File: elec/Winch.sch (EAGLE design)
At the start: 7 parts, among them IC1 LM311D

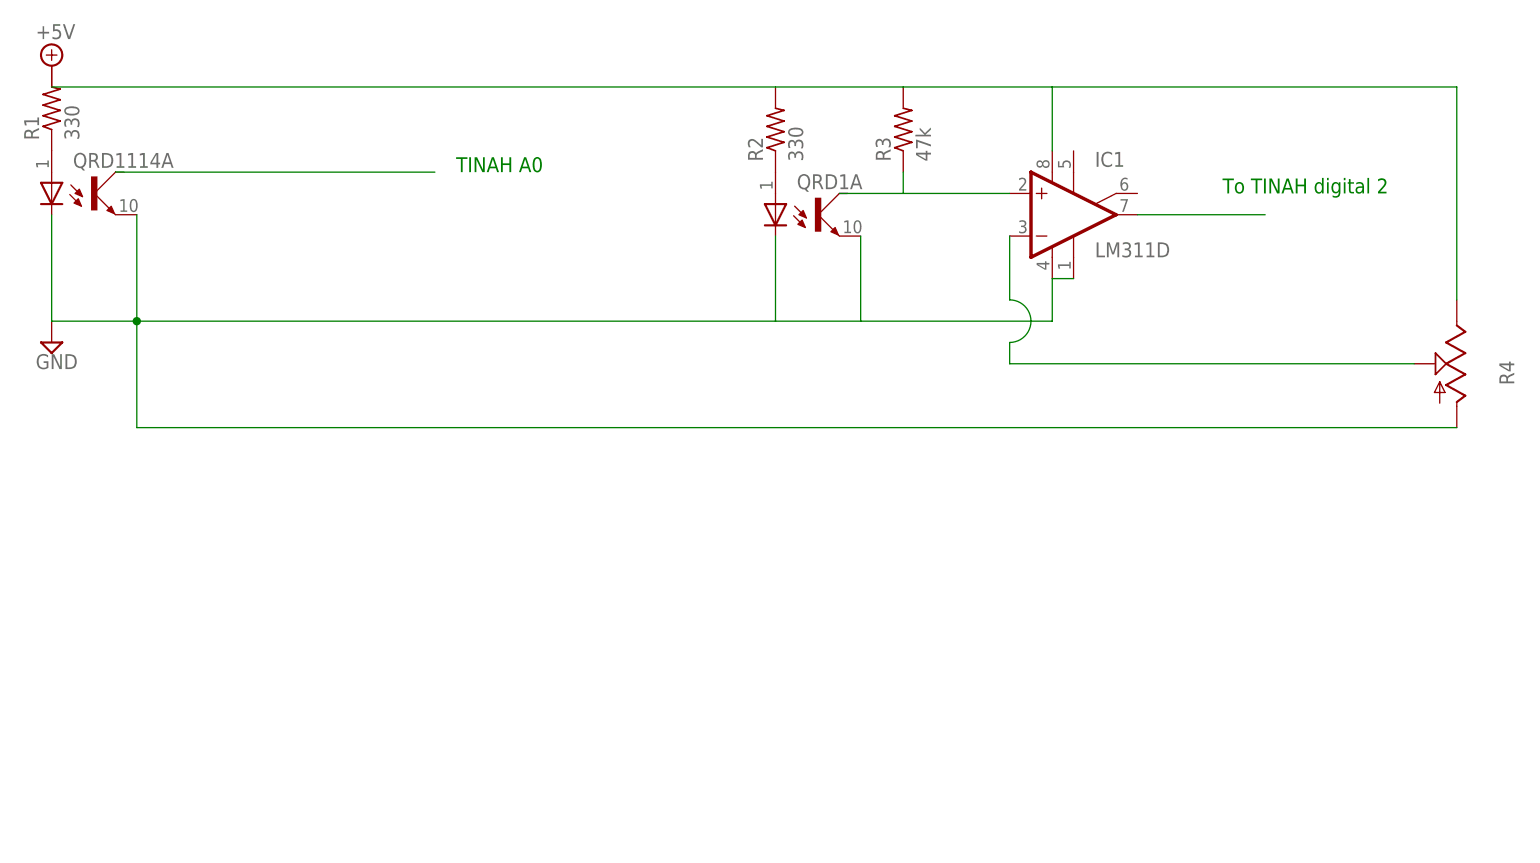
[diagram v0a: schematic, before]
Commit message: Updated QRD and created winch circuit
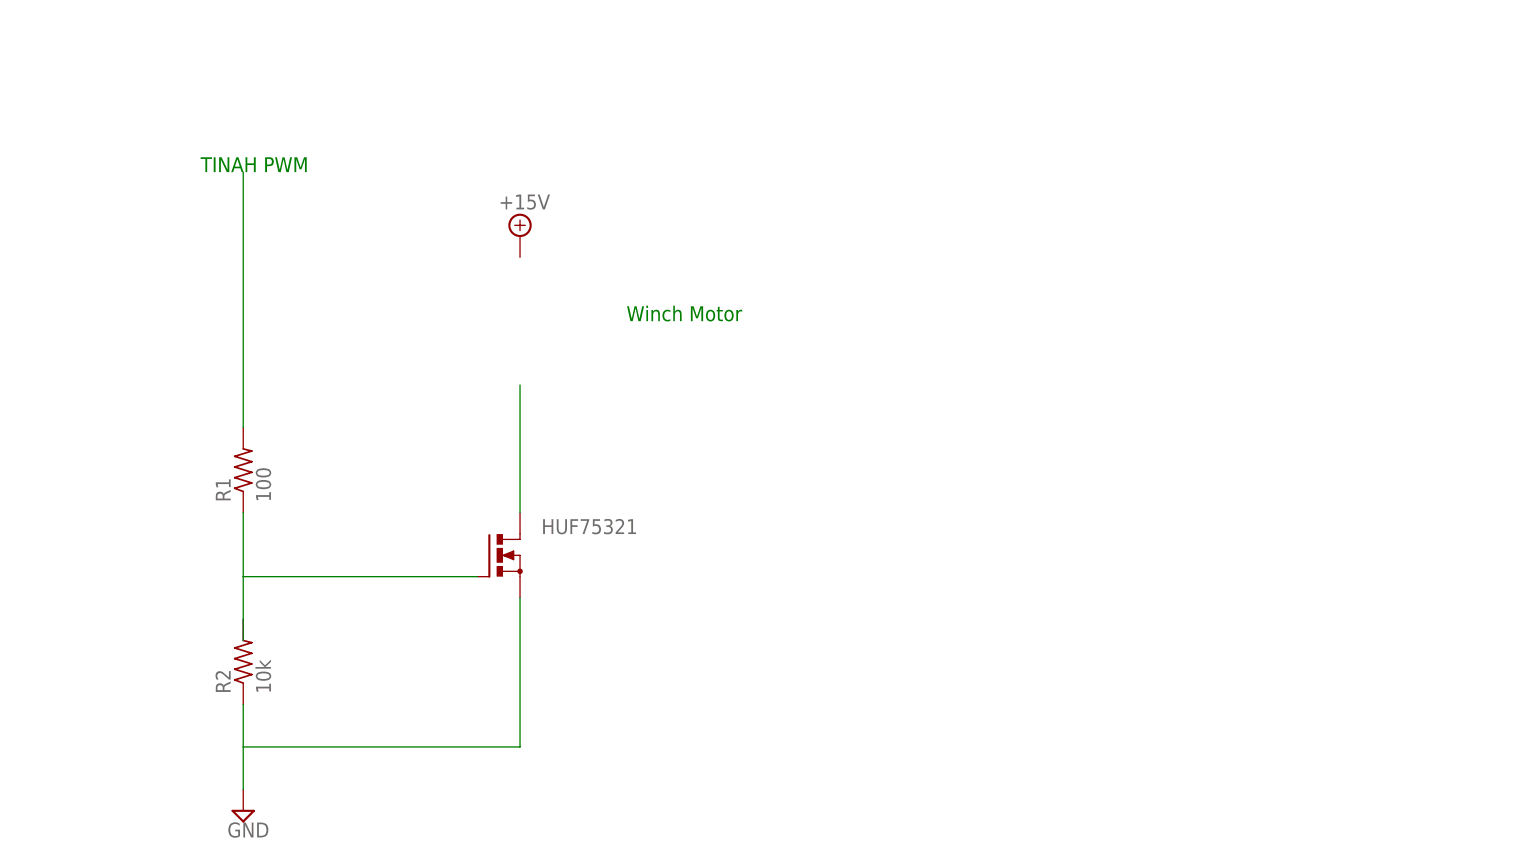
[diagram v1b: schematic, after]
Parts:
- removed IC1: LM311D, linear:LM311D
- removed QRD1, QRD1114: SFH6943, opto-vishay:SFH6943
- removed R3: 47k, resistor:R-US_0204/2V
- removed R4: (no value), pot:TRIM_US-3223G
- added HUF75321: (no value), transistor-power:N-MOSFET-SO8S
- R1: value 330 -> 100
- R2: value 330 -> 10k
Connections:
- removed net +5V: IC1.V+, R2.2, R3.2, R4.E
- removed net N$4: IC1.-IN, R4.S
- removed net N$5: IC1.+IN, R3.1
- removed net N$7: IC1.OUT
- new net N$1: R1.2
- net GND: now also HUF75321.S, R2.1; no longer IC1.GND, IC1.V-, QRD1114A.EMI, QRD1A.EMI, R4.A
- net N$2: now also HUF75321.G, R2.2; no longer QRD1114A.A
- net N$3: now also HUF75321.D; no longer QRD1A.A, R2.1
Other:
- note added: "TINAH PWM"
- note added: "Winch Motor"
- note removed: "TINAH A0"
- note removed: "To TINAH digital 2"
- moved on the sheet: R1, R2
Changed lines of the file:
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@@
 <layer number="48" name="Document" color="7" fill="1" visible="no" active="no"/>
 <layer number="49" name="Reference" color="7" fill="1" visible="no" active="no"/>
-<layer number="51" name="tDocu" color="6" fill="1" visible="no" active="no"/>
+<layer number="51" name="tDocu" color="7" fill="1" visible="no" active="no"/>
 <layer number="52" name="bDocu" color="7" fill="1" visible="no" active="no"/>
-<layer number="57" name="t3D" color="6" fill="5" visible="no" active="no"/>
-<layer number="58" name="b3D" color="5" fill="4" visible="no" active="no"/>
 <layer number="90" name="Modules" color="5" fill="1" visible="yes" active="yes"/>
 <layer number="91" name="Nets" color="2" fill="1" visible="yes" active="yes"/>
@@
 </classes>
 <parts>
-<part name="QRD1114" library="opto-vishay" deviceset="SFH6943" device="" value=""/>
+<part name="R1" library="resistor" deviceset="R-US_" device="0204/2V" value="100"/>
+<part name="R2" library="resistor" deviceset="R-US_" device="0204/2V" value="10k"/>
 <part name="SUPPLY1" library="supply2" deviceset="GND" device=""/>
-<part name="R1" library="resistor" deviceset="R-US_" device="0204/2V" value="330"/>
-<part name="SUPPLY2" library="supply2" deviceset="+5V" device=""/>
-<part name="R2" library="resistor" deviceset="R-US_" device="0204/2V" value="330"/>
-<part name="QRD1" library="opto-vishay" deviceset="SFH6943" device="" value=""/>
-<part name="R3" library="resistor" deviceset="R-US_" device="0204/2V" value="47k"/>
-<part name="IC1" library="linear" deviceset="LM311" device="D"/>
-<part name="R4" library="pot" deviceset="TRIM_US-" device="3223G"/>
+<part name="HUF75321" library="transistor-power" deviceset="N-MOSFET-SO8" device="S"/>
+<part name="SUPPLY2" library="supply2" deviceset="+15V" device=""/>
 </parts>
 <sheets>
 <sheet>
 <plain>
-<text x="20.32" y="86.36" size="1.778" layer="91">TINAH A0</text>
-<text x="111.76" y="83.82" size="1.778" layer="91">To TINAH digital 2</text>
+<text x="-10.16" y="86.36" size="1.778" layer="91">TINAH PWM</text>
+<circle x="27.94" y="68.58" radius="8.032184375" width="0.1524" layer="99"/>
+<text x="40.64" y="68.58" size="1.778" layer="91">Winch Motor</text>
 </plain>
 <instances>
-<instance part="QRD1114" gate="A" x="-27.94" y="83.82"/>
-<instance part="SUPPLY1" gate="GND" x="-27.94" y="66.04"/>
-<instance part="R1" gate="G$1" x="-27.94" y="93.98" rot="R90"/>
-<instance part="SUPPLY2" gate="+5V" x="-27.94" y="99.06"/>
-<instance part="R2" gate="G$1" x="58.42" y="91.44" rot="R90"/>
-<instance part="QRD1" gate="A" x="58.42" y="81.28"/>
-<instance part="R3" gate="G$1" x="73.66" y="91.44" rot="R90"/>
-<instance part="IC1" gate="A" x="93.98" y="81.28"/>
-<instance part="R4" gate="G$1" x="139.7" y="63.5" rot="MR0"/>
+<instance part="R1" gate="G$1" x="-5.08" y="50.8" rot="R90"/>
+<instance part="R2" gate="G$1" x="-5.08" y="27.94" rot="R90"/>
+<instance part="SUPPLY1" gate="GND" x="-5.08" y="10.16"/>
+<instance part="HUF75321" gate="G$1" x="25.4" y="40.64"/>
+<instance part="SUPPLY2" gate="+15V" x="27.94" y="78.74"/>
 </instances>
 <busses>
@@
 <net name="N$1" class="0">
 <segment>
-<wire x1="-20.32" y1="86.36" x2="17.78" y2="86.36" width="0.1524" layer="91"/>
+<wire x1="-5.08" y1="86.36" x2="-5.08" y2="55.88" width="0.1524" layer="91"/>
+<pinref part="R1" gate="G$1" pin="2"/>
+</segment>
+</net>
+<net name="N$2" class="0">
+<segment>
+<pinref part="R1" gate="G$1" pin="1"/>
+<pinref part="R2" gate="G$1" pin="2"/>
+<wire x1="-5.08" y1="45.72" x2="-5.08" y2="38.1" width="0.1524" layer="91"/>
+<wire x1="-5.08" y1="38.1" x2="-5.08" y2="33.02" width="0.1524" layer="91"/>
+<wire x1="-5.08" y1="33.02" x2="-5.08" y2="30.48" width="0.1524" layer="91"/>
+<pinref part="HUF75321" gate="G$1" pin="G"/>
+<wire x1="-5.08" y1="38.1" x2="22.86" y2="38.1" width="0.1524" layer="91"/>
 </segment>
 </net>
 <net name="GND" class="0">
 <segment>
+<pinref part="R2" gate="G$1" pin="1"/>
 <pinref part="SUPPLY1" gate="GND" pin="GND"/>
-<wire x1="-27.94" y1="81.28" x2="-27.94" y2="68.58" width="0.1524" layer="91"/>
-<pinref part="QRD1114" gate="A" pin="EMI"/>
-<wire x1="-27.94" y1="68.58" x2="-17.78" y2="68.58" width="0.1524" layer="91"/>
-<wire x1="-17.78" y1="68.58" x2="-17.78" y2="81.28" width="0.1524" layer="91"/>
-<wire x1="58.42" y1="78.74" x2="58.42" y2="68.58" width="0.1524" layer="91"/>
-<wire x1="58.42" y1="68.58" x2="-17.78" y2="68.58" width="0.1524" layer="91"/>
-<pinref part="QRD1" gate="A" pin="EMI"/>
-<wire x1="58.42" y1="68.58" x2="68.58" y2="68.58" width="0.1524" layer="91"/>
-<wire x1="68.58" y1="68.58" x2="68.58" y2="78.74" width="0.1524" layer="91"/>
-<pinref part="IC1" gate="A" pin="V-"/>
-<pinref part="IC1" gate="A" pin="GND"/>
-<wire x1="93.98" y1="73.66" x2="91.44" y2="73.66" width="0.1524" layer="91"/>
-<wire x1="91.44" y1="73.66" x2="91.44" y2="68.58" width="0.1524" layer="91"/>
-<wire x1="91.44" y1="68.58" x2="68.58" y2="68.58" width="0.1524" layer="91"/>
-<pinref part="R4" gate="G$1" pin="A"/>
-<wire x1="139.7" y1="55.88" x2="-17.78" y2="55.88" width="0.1524" layer="91"/>
-<wire x1="-17.78" y1="55.88" x2="-17.78" y2="68.58" width="0.1524" layer="91"/>
-<junction x="-17.78" y="68.58"/>
-</segment>
-</net>
-<net name="N$2" class="0">
-<segment>
-<pinref part="QRD1114" gate="A" pin="A"/>
-<pinref part="R1" gate="G$1" pin="1"/>
-</segment>
-</net>
-<net name="+5V" class="0">
-<segment>
-<pinref part="SUPPLY2" gate="+5V" pin="+5V"/>
-<wire x1="-27.94" y1="96.52" x2="58.42" y2="96.52" width="0.1524" layer="91"/>
-<pinref part="R2" gate="G$1" pin="2"/>
-<pinref part="R3" gate="G$1" pin="2"/>
-<wire x1="58.42" y1="96.52" x2="73.66" y2="96.52" width="0.1524" layer="91"/>
-<pinref part="IC1" gate="A" pin="V+"/>
-<wire x1="73.66" y1="96.52" x2="91.44" y2="96.52" width="0.1524" layer="91"/>
-<wire x1="91.44" y1="96.52" x2="91.44" y2="88.9" width="0.1524" layer="91"/>
-<pinref part="R4" gate="G$1" pin="E"/>
-<wire x1="139.7" y1="71.12" x2="139.7" y2="96.52" width="0.1524" layer="91"/>
-<wire x1="139.7" y1="96.52" x2="91.44" y2="96.52" width="0.1524" layer="91"/>
+<wire x1="-5.08" y1="22.86" x2="-5.08" y2="17.78" width="0.1524" layer="91"/>
+<pinref part="HUF75321" gate="G$1" pin="S"/>
+<wire x1="-5.08" y1="17.78" x2="-5.08" y2="12.7" width="0.1524" layer="91"/>
+<wire x1="-5.08" y1="17.78" x2="27.94" y2="17.78" width="0.1524" layer="91"/>
+<wire x1="27.94" y1="17.78" x2="27.94" y2="35.56" width="0.1524" layer="91"/>
 </segment>
 </net>
 <net name="N$3" class="0">
 <segment>
-<pinref part="R2" gate="G$1" pin="1"/>
-<pinref part="QRD1" gate="A" pin="A"/>
+<pinref part="HUF75321" gate="G$1" pin="D"/>
+<wire x1="27.94" y1="60.96" x2="27.94" y2="45.72" width="0.1524" layer="91"/>
 </segment>
 </net>
-<net name="N$5" class="0">
-<segment>
-<pinref part="R3" gate="G$1" pin="1"/>
-<wire x1="66.04" y1="83.82" x2="73.66" y2="83.82" width="0.1524" layer="91"/>
-<wire x1="73.66" y1="83.82" x2="73.66" y2="86.36" width="0.1524" layer="91"/>
-<pinref part="IC1" gate="A" pin="+IN"/>
-<wire x1="73.66" y1="83.82" x2="86.36" y2="83.82" width="0.1524" layer="91"/>
-</segment>
-</net>
-<net name="N$4" class="0">
-<segment>
-<pinref part="IC1" gate="A" pin="-IN"/>
-<wire x1="86.36" y1="78.74" x2="86.36" y2="71.12" width="0.1524" layer="91"/>
-<wire x1="86.36" y1="71.12" x2="86.36" y2="66.04" width="0.1524" layer="91" curve="-180"/>
-<pinref part="R4" gate="G$1" pin="S"/>
-<wire x1="134.62" y1="63.5" x2="86.36" y2="63.5" width="0.1524" layer="91"/>
-<wire x1="86.36" y1="63.5" x2="86.36" y2="66.04" width="0.1524" layer="91"/>
-</segment>
-</net>
-<net name="N$7" class="0">
-<segment>
-<pinref part="IC1" gate="A" pin="OUT"/>
-<wire x1="101.6" y1="81.28" x2="116.84" y2="81.28" width="0.1524" layer="91"/>
-</segment>
-</net>

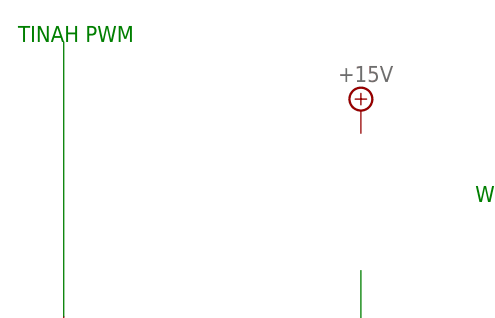
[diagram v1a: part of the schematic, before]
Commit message: modified winch circuit
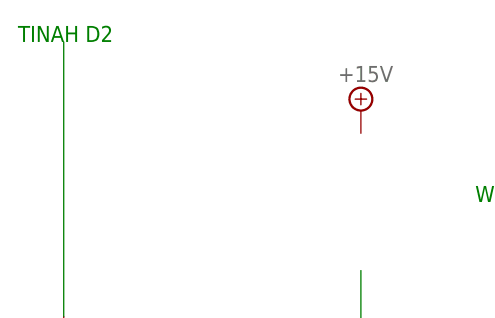
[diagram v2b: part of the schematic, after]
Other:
- note added: "TINAH D2"
- note removed: "TINAH PWM"
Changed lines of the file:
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@@
 <sheet>
 <plain>
-<text x="-10.16" y="86.36" size="1.778" layer="91">TINAH PWM</text>
+<text x="-10.16" y="86.36" size="1.778" layer="91">TINAH D2</text>
 <circle x="27.94" y="68.58" radius="8.032184375" width="0.1524" layer="99"/>
 <text x="40.64" y="68.58" size="1.778" layer="91">Winch Motor</text>
